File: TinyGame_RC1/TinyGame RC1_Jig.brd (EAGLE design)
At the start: 38 x 22 mm, 41 parts, among them J1 AUDIO-CONNECTOR-6P-SMD-344003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, K1 BUTTON-4P-3100010P1, K2 BUTTON-4P-3100010P1, K3 BUTTON-4P-3100010P1, K4 BUTTON-4P-3100010P1, U1 MKL02Z32VFK4

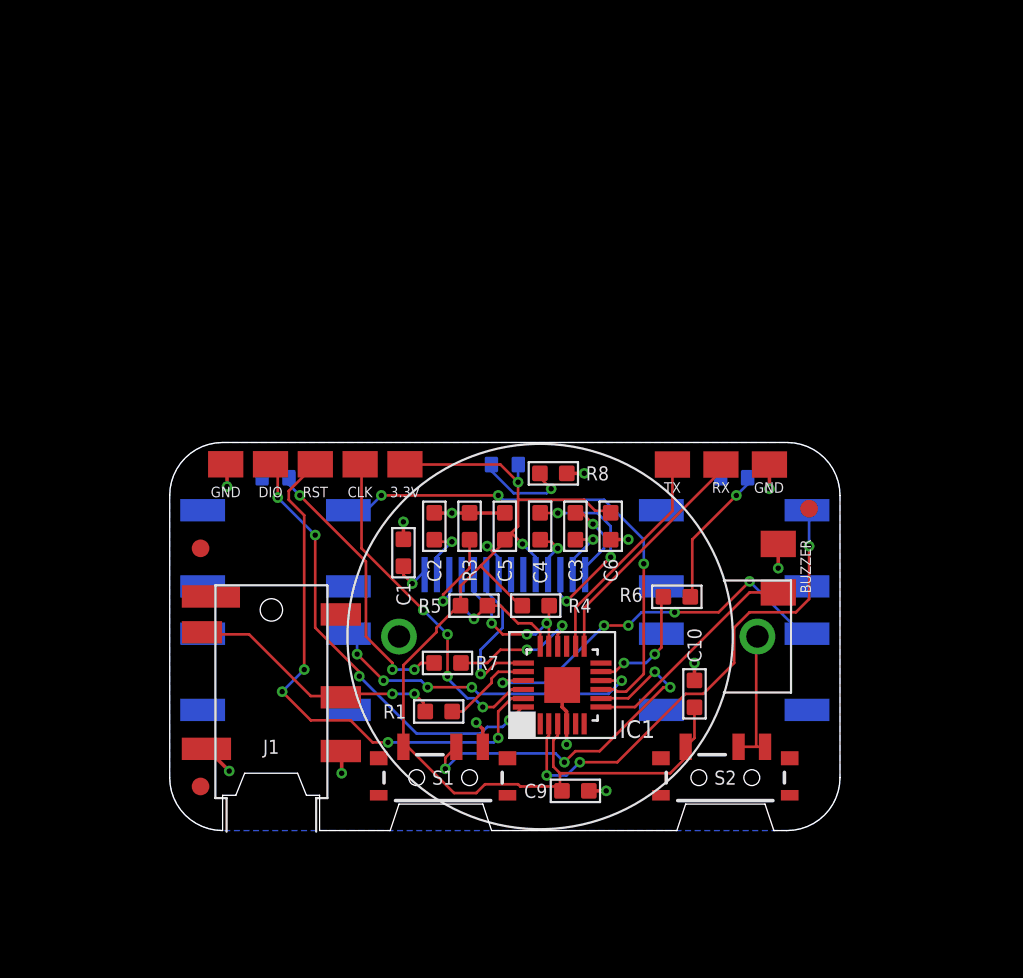
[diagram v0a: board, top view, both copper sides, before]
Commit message: Moved some stuff around - added testjig and jtag adapter
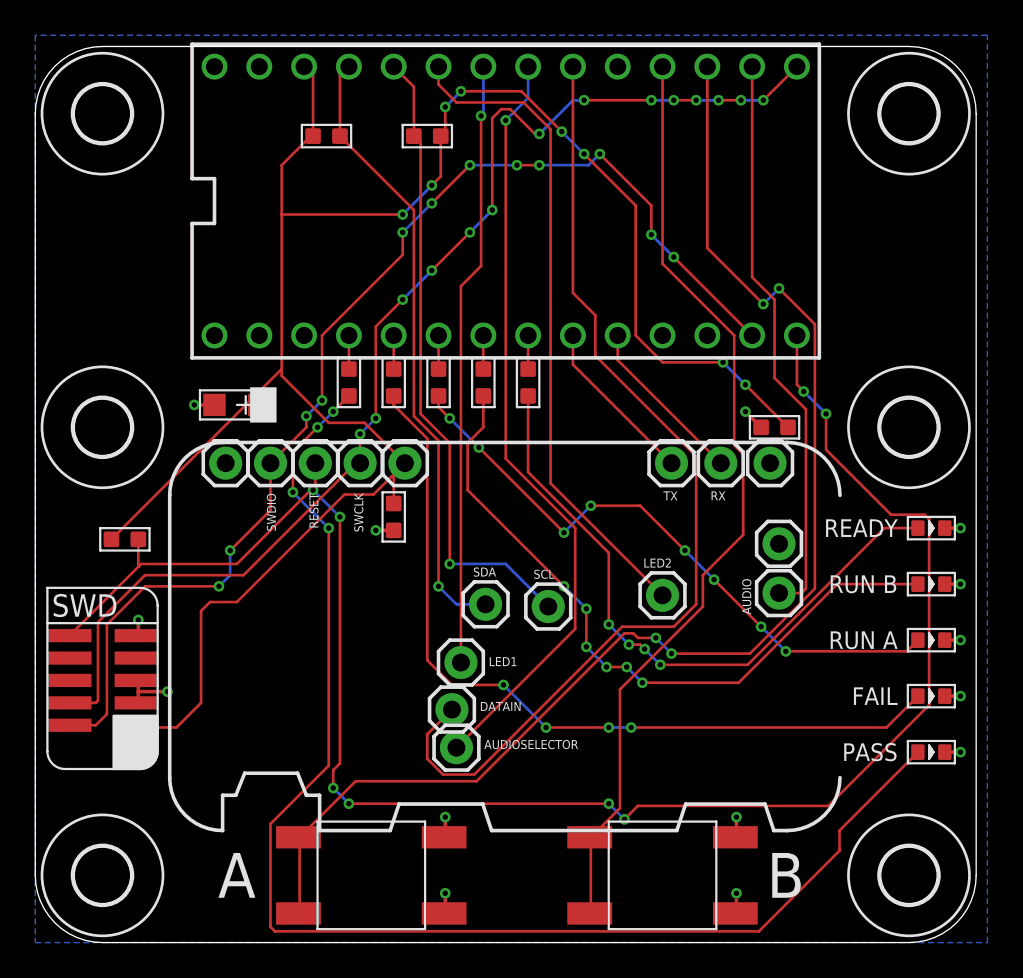
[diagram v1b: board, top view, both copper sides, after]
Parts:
- removed AUDIOGND, AUDIOSIG, PTA6_MISO1, PTA6_MISO2, PTA6_MISO3, PTA6_MISO4, PTA6_MISO5, PTB1_RXTX, PTB2_TXRX, PTB2_TXRX2: M01SMD-4.5X1.5, SparkFun-Connectors:PAD-1.5X4.5
- removed BATTERY_1: BATTERY_1236_C, MicroGameboyParts:BATTERY_1236_C
- removed C10: 100nF, OPL:C0603
- removed C3, C5, C6, C9: 1uF, OPL:C0603
- removed J1: AUDIO-CONNECTOR-6P-SMD-3440030P1, OPL:6P-SMD-3.5
- removed K3, K4: BUTTON-4P-3100010P1, zephod-components:4P-SMD-6.0X6.0X5.0H
- removed S1, S2: (no value), SparkFun-Electromechanical:SWITCH-SPST-SMD-A
- removed U$2, U$3, U$4: FIDUCIAL, adafruit:FIDUCIAL_1MM
- removed U1: MKL02Z32VFK4, FarnellThings:QFN50P400X400X100-25N
- added 3.3V_1, AUDIO, AUDIOSELECTOR, DATAIN, GND_1, GND_2, GND_3, LED1, LED2, RESET, RX, SCL, SDA, SWCLK, SWDIO, TX: M01PTH, SparkFun-Connectors:1X01
- added D4, D5: (no value), OPL:LED0603
- added H1, H2, H3, H4, H5, H6: MOUNT-HOLE3.2, zephod-components:3,2
- added R2: 2K, OPL:R0603
- added SWD1: CORTEX_SWDVERT, carrilib with jtags:SWD_VERTICAL
- C1: value 2.2uF -> (none)
- C2: value 4.7uF -> (none)
- C4: value 1uF -> (none); device OPL:C0603 -> OPL:AVX-A
- D1, D2, D3: value YELLOW -> (none)
- K1, K2: device zephod-components:4P-SMD-6.0X6.0X5.0H -> OPL:4P-SMD-6.0X6.0X5.0H
- R3: value 390K -> 2K
- R8: value 2K -> 10K
- U$1: value 0.49"OLEDFOLDED -> TEENSY_LC_DIL; device zephod-tft:0.49"-FPC-0.7-14-FOLDED -> Teensy_3_and_LC_Series_Boards_v1.4:TEENSY_3.0-3.2&LC_DIL
- moved D2 39.2 mm to (43.2, 7.62), flipped to the top
- moved R5 27.9 mm to (8.89, 39.4)
- moved K1 27.7 mm to (11.4, -2.54), flipped to the top
- moved R4 27.3 mm to (14.6, 39.4), turned to 0 degrees
- moved D3 26.1 mm to (43.2, 10.8), flipped to the top
- moved R8 24.6 mm to (-2.54, 16.5)
- moved C1 22.2 mm to (34.3, 22.9), turned to 0 degrees
- moved U$1 19.7 mm to (19.1, 35.7), flipped to the top, turned to 90 degrees
- moved R1 19.3 mm to (10.2, 25.4), turned to 270 degrees
- moved D1 19.2 mm to (43.2, 4.45), flipped to the top
- moved C4 18.5 mm to (3.81, 24.1), turned to 180 degrees
- moved R7 16.5 mm to (20.3, 25.4), turned to 270 degrees
- moved R6 16.4 mm to (17.8, 25.4), turned to 270 degrees
- moved K2 12.2 mm to (27.9, -2.54), flipped to the top
- moved R3 8.34 mm to (15.2, 25.4)
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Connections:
- removed net AUDIO: AUDIOSIG.P$1, U1.7
- removed net AUDIOSELECTOR: S1.2, U1.8
- removed net BUTTON1: K1.1, U1.2
- removed net BUTTON2: K3.1, U1.9
- removed net BUTTON3: K4.1, U1.10
- removed net BUTTON4: K2.1, U1.21
- removed net DATAIN: R1.2, U1.20
- removed net LED1: R6.2, U1.11
- removed net LED2: R7.2, U1.16
- removed net OLED_RESET: U$1.P$9, U1.19
- removed net OLED_SCL: R4.1, U$1.P$10, U1.17
- removed net OLED_SDA: R5.1, U$1.P$11, U1.18
- removed net PTB1: PTB1_RXTX.P$1, U1.13
- removed net PTB2: PTB2_TXRX.P$1, U1.14
- new net N$15: R7.1, U$1.6
- new net N$16: D1.+, R1.2
- new net N$17: D2.+, R2.2
- new net N$18: D3.+, R3.2
- new net N$21: K1.0A, K1.1A, U$1.15/A1
- new net N$22: K2.0A, K2.1A, U$1.16/A2
- new net N$8: LED1.1, U$1.20/A6
- new net SCL: R4.1, SCL.1, U$1.22/A8
- new net SDA: R5.1, SDA.1, U$1.23/A9
- new net VIN: U$1.VIN
- net 3.3V: now also 3.3V_1.1, C1.2, C2.2, C4.+, R8.2, SWD1.1, U$1.3.3V; no longer C10.2, C5.2, C6.2, C9.2, D3.+, PTA6_MISO1.P$1, S1.3, S2.3, U$1.P$5, U$1.P$8, U1.3
- net GND: now also C1.1, C4.-, D3.-, D4.-, D5.-, GND_1.1, GND_2.1, GND_3.1, K1.0B, K1.1B, K2.0B, K2.1B, SWD1.3, SWD1.5, SWD1.9, U$1.AGND, U$1.GND; no longer AUDIOGND.P$1, BATTERY_1.-, C1.2, C10.1, C5.1, C6.1, C9.1, J1.COM1, J1.COM2, K1.2, K1.3, K2.2, K2.3, K3.2, K3.3, K4.2, K4.3, PTA6_MISO5.P$1, PTB2_TXRX2.P$1, R3.1, R8.1, S1.1, U$1.P$7, U1.25, U1.4
- net N$10: now also DATAIN.1, U$1.18/A4; no longer C1.1, U$1.P$14
- net N$11: now also R1.1, U$1.2; no longer C2.2, U$1.P$13
- net N$12: now also R2.1, U$1.3; no longer C3.1, U$1.P$2
- net N$13: now also R3.1, U$1.4; no longer C4.1, U$1.P$4
- net N$14: now also R6.1, U$1.5; no longer D2.+, R7.1
- net N$19: now also D4.+, R6.2; no longer D3.-, R8.2
- net N$2: now also TX.1, U$1.7; no longer J1.L, J1.R, R1.1
- net N$20: now also D5.+, R7.2; no longer BATTERY_1.+, S2.1, S2.2
- net N$3: now also RX.1, U$1.8; no longer C3.2, U$1.P$1
- net N$4: now also AUDIO.1, U$1.14/A0; no longer C4.2, U$1.P$3
- net N$6: now also LED2.1, U$1.21/A7; no longer D1.+, R6.1
- net N$9: now also AUDIOSELECTOR.1, U$1.19/A5; no longer R3.2, U$1.P$12
- net RESET: now also R8.1, RESET.1, SWD1.10, U$1.12; no longer PTA6_MISO4.P$1, U1.23
- net SWCLK: now also SWCLK.1, SWD1.4, U$1.13; no longer PTA6_MISO3.P$1, U1.22
- net SWDIO: now also SWD1.2, SWDIO.1, U$1.11; no longer PTA6_MISO2.P$1, U1.24
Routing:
- net N$16: track 0.00 -> 75.3 mm, vias 0 -> 4
- net N$21: track 0.00 -> 74.3 mm, vias 0 -> 4
- net RESET: track 31.2 -> 100.5 mm, vias 4 -> 8
- net N$10: track 2.22 -> 56.4 mm, vias 1 -> 0
- net N$22: track 0.00 -> 53.6 mm
- net 3.3V: track 65.7 -> 113.9 mm, vias 3 -> 8
- net SWCLK: track 19.6 -> 67.0 mm, vias 4 -> 14
- net N$17: track 0.00 -> 45.9 mm, vias 0 -> 4
- net SWDIO: track 25.4 -> 66.0 mm, vias 4 -> 12
- net N$9: track 5.79 -> 43.6 mm
- net SCL: track 0.00 -> 36.1 mm, vias 0 -> 1
- net SDA: track 0.00 -> 35.1 mm, vias 0 -> 1
- net N$18: track 0.00 -> 35.1 mm, vias 0 -> 8
- net N$8: track 0.00 -> 34.3 mm, vias 0 -> 1
- net N$19: track 5.53 -> 39.3 mm, vias 1 -> 6
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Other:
- board size 38 x 22 mm -> 53.3 x 50.8 mm
- board text added: "A"
- board text added: "B"
- board text added: "FAIL"
- board text added: "PASS"
- board text added: "READY"
- board text added: "RUN A"
- board text added: "RUN B"
- board text removed: "3.3V"
- board text removed: "BUZZER"
- board text removed: "CLK"
- board text removed: "DIO"
- board text removed: "GND"
- board text removed: "IC1"
- board text removed: "RST"
- board text removed: "RX"
- board text removed: "TX"
- board text removed: "TinyGame"

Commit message: Artwork and gerbers
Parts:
- added U$2: TINRS_ARTWORKLOGO, EurorackModularParts:TINRSLOGO
- added U$3: TINRS_ARTWORKROCKET, EurorackModularParts:TINRS_ROCKET
